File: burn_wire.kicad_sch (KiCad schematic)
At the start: 12 parts, among them Q4 Q_PI, Q5 TIP122, Q6 Q_NPN_BEC

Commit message: Edits to board post PDR.
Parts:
- added R21: 10 kohm, symbol Device:R_US
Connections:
- net GND: now also D7.1 (K)
- net at D5.2 (A2), Q5.2 (C), R8.1: now also R21.1
- net at D7.2 (A): now also R21.2
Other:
- note added: "LED on when Q5 is on (burn-wire active)."
- moved on the sheet: D7
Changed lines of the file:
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@@
+		)
+	)
+	(text "LED on when Q5 is on (burn-wire active)."
+		(exclude_from_sim no)
+		(at 153.162 83.312 0)
+		(effects
+			(font
+				(size 1.27 1.27)
+			)
 		)
 	)
@@
 		(color 0 0 0 0)
 	)
+	(junction
+		(at 116.84 78.74)
+		(diameter 0)
+		(color 0 0 0 0)
+	)
 	(wire
 		(pts
@@
 	(wire
 		(pts
+			(xy 116.84 78.74) (xy 116.84 87.63)
+		)
+		(stroke
+			(width 0)
+			(type default)
+		)
+	)
+	(wire
+		(pts
 			(xy 116.84 106.68) (xy 116.84 97.79)
 		)
@@
 	(wire
 		(pts
+			(xy 116.84 78.74) (xy 120.65 78.74)
+		)
+		(stroke
+			(width 0)
+			(type default)
+		)
+	)
+	(wire
+		(pts
 			(xy 54.61 74.93) (xy 54.61 95.25)
 		)
@@
 	(wire
 		(pts
+			(xy 128.27 78.74) (xy 133.35 78.74)
+		)
+		(stroke
+			(width 0)
+			(type default)
+		)
+	)
+	(wire
+		(pts
 			(xy 68.58 82.55) (xy 74.93 82.55)
 		)
@@
 	(wire
 		(pts
-			(xy 116.84 58.42) (xy 116.84 87.63)
+			(xy 140.97 78.74) (xy 148.59 78.74)
+		)
+		(stroke
+			(width 0)
+			(type default)
+		)
+	)
+	(wire
+		(pts
+			(xy 116.84 58.42) (xy 116.84 78.74)
 		)
 		(stroke
@@
 			(width 0)
 			(type default)
+		)
+	)
+	(global_label "GND"
+		(shape input)
+		(at 148.59 78.74 0)
+		(fields_autoplaced yes)
+		(effects
+			(font
+				(size 1.27 1.27)
+			)
+			(justify left)
+		)
+		(property "Intersheetrefs" "${INTERSHEET_REFS}"
+			(at 155.4457 78.74 0)
+			(effects
+				(font
+					(size 1.27 1.27)
+				)
+				(justify left)
+				(hide yes)
+			)
 		)
 	)
@@
 	)
 	(symbol
+		(lib_id "Device:R_US")
+		(at 124.46 78.74 90)
+		(unit 1)
+		(exclude_from_sim no)
+		(in_bom yes)
+		(on_board yes)
+		(dnp no)
+		(property "Reference" "R21"
+			(at 126.365 84.4551 90)
+			(effects
+				(font
+					(size 1.27 1.27)
+				)
+				(justify left)
+			)
+		)
+		(property "Value" "10 kohm"
+			(at 128.016 81.788 90)
+			(effects
+				(font
+					(size 1.27 1.27)
+				)
+				(justify left)
+			)
+		)
+		(property "Footprint" ""
+			(at 124.714 77.724 90)
+			(effects
+				(font
+					(size 1.27 1.27)
+				)
+				(hide yes)
+			)
+		)
+		(property "Datasheet" "~"
+			(at 124.46 78.74 0)
+			(effects
+				(font
+					(size 1.27 1.27)
+				)
+				(hide yes)
+			)
+		)
+		(property "Description" "Resistor, US symbol"
+			(at 124.46 78.74 0)
+			(effects
+				(font
+					(size 1.27 1.27)
+				)
+				(hide yes)
+			)
+		)
+		(pin "2"
+		)
+		(pin "1"
+		)
+		(instances
+			(project "deck_board"
+				(path "/0dd6c749-d328-44a2-b3d4-206fc5899db9/9a513996-12e6-4869-a836-62e374407735"
+					(reference "R21")
+					(unit 1)
+				)
+			)
+		)
+	)
+	(symbol
 		(lib_id "Transistor_BJT:Q_NPN_BEC")
 		(at 88.9 73.66 270)
@@
 	(symbol
 		(lib_id "Device:LED")
-		(at 127 50.8 0)
+		(at 137.16 78.74 180)
 		(unit 1)
 		(exclude_from_sim no)
@@
 		(fields_autoplaced yes)
 		(property "Reference" "D7"
-			(at 125.4125 44.45 0)
+			(at 138.7475 71.12 0)
 			(effects
 				(font
@@
 		)
 		(property "Value" "LED"
-			(at 125.4125 46.99 0)
+			(at 138.7475 73.66 0)
 			(effects
 				(font
@@
 		)
 		(property "Footprint" ""
-			(at 127 50.8 0)
+			(at 137.16 78.74 0)
 			(effects
 				(font
@@
 		)
 		(property "Datasheet" "~"
-			(at 127 50.8 0)
+			(at 137.16 78.74 0)
 			(effects
 				(font
@@
 		)
 		(property "Description" "Light emitting diode"
-			(at 127 50.8 0)
+			(at 137.16 78.74 0)
 			(effects
 				(font
@@
 		)
 		(property "Sim.Pins" "1=K 2=A"
-			(at 127 50.8 0)
-			(effects
-				(font
+			(at 137.16 78.74 0)
+			(effects
+				(font

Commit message: Updated files and include work done for PCB
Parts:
- D7: footprint (none) -> LED_SMD:LED_0603_1608Metric
- F3: footprint (none) -> Fuse:Fuse_1812_4532Metric
- Q4, Q6: footprint (none) -> Package_TO_SOT_SMD:SOT-23
- R10, R11, R12, R13, R14, R21, R8: footprint (none) -> Resistor_SMD:R_0201_0603Metric
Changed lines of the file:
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@@
 			)
 		)
-		(property "Footprint" ""
+		(property "Footprint" "Fuse:Fuse_1812_4532Metric"
 			(at 78.74 56.642 90)
 			(effects
@@
 			)
 		)
-		(property "Footprint" ""
+		(property "Footprint" "Resistor_SMD:R_0201_0603Metric"
 			(at 64.516 88.646 90)
 			(effects
@@
 			)
 		)
-		(property "Footprint" ""
+		(property "Footprint" "Resistor_SMD:R_0201_0603Metric"
 			(at 124.714 77.724 90)
 			(effects
@@
 			)
 		)
-		(property "Footprint" ""
+		(property "Footprint" "Package_TO_SOT_SMD:SOT-23"
 			(at 91.44 78.74 0)
 			(effects
@@
 			)
 		)
-		(property "Footprint" ""
+		(property "Footprint" "LED_SMD:LED_0603_1608Metric"
 			(at 137.16 78.74 0)
 			(effects
@@
 			)
 		)
-		(property "Footprint" ""
+		(property "Footprint" "Resistor_SMD:R_0201_0603Metric"
 			(at 64.516 83.566 90)
 			(effects
@@
 			)
 		)
-		(property "Footprint" ""
+		(property "Footprint" "Resistor_SMD:R_0201_0603Metric"
 			(at 96.266 59.436 90)
 			(effects
@@
 			)
 		)
-		(property "Footprint" ""
+		(property "Footprint" "Resistor_SMD:R_0201_0603Metric"
 			(at 77.216 93.726 90)
 			(effects
@@
 			)
 		)
-		(property "Footprint" ""
+		(property "Footprint" "Resistor_SMD:R_0201_0603Metric"
 			(at 96.774 98.806 90)
 			(effects
@@
 			)
 		)
-		(property "Footprint" ""
+		(property "Footprint" "Package_TO_SOT_SMD:SOT-23"
 			(at 77.47 72.39 0)
 			(effects
@@
 			)
 		)
-		(property "Footprint" ""
+		(property "Footprint" "Resistor_SMD:R_0201_0603Metric"
 			(at 55.626 99.314 90)
 			(effects

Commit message: PCB is mostly laid out, routing is WIP
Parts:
- removed D5: SMAJ33A, Diode_SMD:D_SMA, symbol Diode:SMAJ33A
- removed F3: Fuse, Fuse:Fuse_1812_4532Metric, symbol Device:Fuse
- removed Q4: Q_PI, Package_TO_SOT_SMD:SOT-23, symbol Transistor_BJT:Q_NPN_BEC
- removed Q5: TIP122, Package_TO_SOT_THT:TO-220-3_Vertical, symbol Transistor_BJT:TIP122
- removed Q6: Q_NPN_BEC, Package_TO_SOT_SMD:SOT-23, symbol Transistor_BJT:Q_NPN_BEC
- removed R12, R13, R14: R, Resistor_SMD:R_0201_0603Metric, symbol Device:R_US
- added C13: 0.1 µF, Capacitor_SMD:C_0603_1608Metric, symbol Device:C
- added F2: 1.0 A, Fuse:Fuse_1812_4532Metric, symbol Device:Fuse
- added Q5: NMOS, Package_TO_SOT_SMD:SOT-23, symbol Simulation_SPICE:NMOS
- added R24: 158Ω, Resistor_SMD:R_0201_0603Metric, symbol Device:R_US
- added R9: 100kΩ, Resistor_SMD:R_0201_0603Metric, symbol Device:R_US
- added U5: 74LVC1G08, Package_TO_SOT_SMD:SOT-23-5, symbol 74xGxx:74LVC1G08
- R10: value R -> 47Ω
- R11, R8: value R -> 100kΩ
- R21: value 10 kohm -> 10kΩ
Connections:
- net 3V_IN: now also U5.5 (VCC); no longer R10.2
- net CTRL_IN: now also R9.1, U5.1
- net ENABLE: now also R8.1, U5.2
- net GND: now also R8.2, C13.2, Q5.3 (S), R9.2; no longer D7.1 (K)
- net V_IN_28V: now also F2.2
- net at R21.1: now also R24.1; no longer R8.1
- net at R10.1, R11.2: now also Q5.2 (G)
- new net: D7.1 (K), Q5.1 (D)
- new net: C13.1, U5.3 (GND)
- new net: R10.2, U5.4
- new net: F2.1, R24.2
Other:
- note removed: "clamp transient voltage from burn element"
- note removed: "limit current"
- note removed: "low-side switch when base gets current, allows current to flow through R8"
- note removed: "pull-up"
- note removed: "when pi outputs high, conducts"
- note removed: "when signal from inhibit is high, conducts"

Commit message: Finished PCB, ready to print
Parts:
- added J2, J3: Conn_01x01_Pin, Connector_Wire:SolderWire-0.75sqmm_1x01_D1.25mm_OD2.3mm, symbol Connector:Conn_01x01_Pin
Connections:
- net at R21.1, R24.1: now also J3.1 (Pin_1)
- net at F2.1, R24.2: now also J2.1 (Pin_1)
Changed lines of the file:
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@@
+	)
+	(junction
+		(at 90.17 52.07)
+		(diameter 0)
+		(color 0 0 0 0)
 	)
 	(junction
@@
 	)
 	(junction
+		(at 110.49 52.07)
+		(diameter 0)
+		(color 0 0 0 0)
+	)
+	(junction
 		(at 119.38 95.25)
 		(diameter 0)
@@
 	(wire
 		(pts
+			(xy 90.17 52.07) (xy 97.79 52.07)
+		)
+		(stroke
+			(width 0)
+			(type default)
+		)
+	)
+	(wire
+		(pts
 			(xy 119.38 88.9) (xy 119.38 95.25)
 		)
@@
 	(wire
 		(pts
-			(xy 60.96 52.07) (xy 97.79 52.07)
+			(xy 60.96 52.07) (xy 90.17 52.07)
 		)
 		(stroke
@@
 	(wire
 		(pts
+			(xy 110.49 50.8) (xy 110.49 52.07)
+		)
+		(stroke
+			(width 0)
+			(type default)
+		)
+	)
+	(wire
+		(pts
 			(xy 101.6 74.93) (xy 105.41 74.93)
 		)
@@
 	(wire
 		(pts
+			(xy 110.49 52.07) (xy 105.41 52.07)
+		)
+		(stroke
+			(width 0)
+			(type default)
+		)
+	)
+	(wire
+		(pts
 			(xy 133.35 60.96) (xy 133.35 59.69)
 		)
@@
 	(wire
 		(pts
+			(xy 90.17 50.8) (xy 90.17 52.07)
+		)
+		(stroke
+			(width 0)
+			(type default)
+		)
+	)
+	(wire
+		(pts
 			(xy 69.85 87.63) (xy 69.85 95.25)
 		)
@@
 	(wire
 		(pts
-			(xy 133.35 52.07) (xy 105.41 52.07)
+			(xy 133.35 52.07) (xy 110.49 52.07)
 		)
 		(stroke
@@
 			)
 			(justify right)
+		)
+	)
+	(symbol
+		(lib_id "Connector:Conn_01x01_Pin")
+		(at 110.49 45.72 270)
+		(unit 1)
+		(exclude_from_sim no)
+		(in_bom yes)
+		(on_board yes)
+		(dnp no)
+		(fields_autoplaced yes)
+		(property "Reference" "J3"
+			(at 111.76 45.0849 90)
+			(effects
+				(font
+					(size 1.27 1.27)
+				)
+				(justify left)
+			)
+		)
+		(property "Value" "Conn_01x01_Pin"
+			(at 111.76 47.6249 90)
+			(effects
+				(font
+					(size 1.27 1.27)
+				)
+				(justify left)
+			)
+		)
+		(property "Footprint" "Connector_Wire:SolderWire-0.75sqmm_1x01_D1.25mm_OD2.3mm"
+			(at 110.49 45.72 0)
+			(effects
+				(font
+					(size 1.27 1.27)
+				)
+				(hide yes)
+			)
+		)
+		(property "Datasheet" "~"
+			(at 110.49 45.72 0)
+			(effects
+				(font
+					(size 1.27 1.27)
+				)
+				(hide yes)
+			)
+		)
+		(property "Description" "Generic connector, single row, 01x01, script generated"
+			(at 110.49 45.72 0)
+			(effects
+				(font
+					(size 1.27 1.27)
+				)
+				(hide yes)
+			)
+		)
+		(pin "1"
+		)
+		(instances
+			(project "deck_boardv1.2"
+				(path "/0dd6c749-d328-44a2-b3d4-206fc5899db9/9a513996-12e6-4869-a836-62e374407735"
+					(reference "J3")
+					(unit 1)
+				)
+			)
 		)
 	)
@@
 					(unit 1)
 				)
+			)
+		)
+	)
+	(symbol
+		(lib_id "Connector:Conn_01x01_Pin")
+		(at 90.17 45.72 270)
+		(unit 1)
+		(exclude_from_sim no)
+		(in_bom yes)
+		(on_board yes)
+		(dnp no)
+		(fields_autoplaced yes)
+		(property "Reference" "J2"
+			(at 91.44 45.0849 90)
+			(effects
+				(font
+					(size 1.27 1.27)
+				)
+				(justify left)
+			)
+		)
+		(property "Value" "Conn_01x01_Pin"
+			(at 91.44 47.6249 90)
+			(effects
+				(font
+					(size 1.27 1.27)
+				)
+				(justify left)
+			)
+		)
+		(property "Footprint" "Connector_Wire:SolderWire-0.75sqmm_1x01_D1.25mm_OD2.3mm"
+			(at 90.17 45.72 0)
+			(effects
+				(font
+					(size 1.27 1.27)
+				)
+				(hide yes)
+			)
+		)
+		(property "Datasheet" "~"
+			(at 90.17 45.72 0)
+			(effects
+				(font
+					(size 1.27 1.27)
+				)
+				(hide yes)
+			)
+		)
+		(property "Description" "Generic connector, single row, 01x01, script generated"
+			(at 90.17 45.72 0)
+			(effects
+				(font
+					(size 1.27 1.27)
+				)
+				(hide yes)
+			)
+		)
+		(pin "1"
+		)
+		(instances
+			(project ""
+				(path "/0dd6c749-d328-44a2-b3d4-206fc5899db9/9a513996-12e6-4869-a836-62e374407735"
+					(reference "J2")
+					(unit 1)
+				)

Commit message: Made changes to schematic
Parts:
- removed C13: 0.1 µF, Capacitor_SMD:C_0603_1608Metric, symbol Device:C
- removed F2: 1.0 A, Fuse:Fuse_1812_4532Metric, symbol Device:Fuse
- removed R10: 47Ω, Resistor_SMD:R_0201_0603Metric, symbol Device:R_US
- removed R11, R8, R9: 100kΩ, Resistor_SMD:R_0201_0603Metric, symbol Device:R_US
- removed U5: 74LVC1G08, Package_TO_SOT_SMD:SOT-23-5, symbol 74xGxx:74LVC1G08
- added R2: 100kΩ, Resistor_SMD:R_0201_0603Metric, symbol Device:R_US
- R21: value 10kΩ -> 1.8kΩ
- R24: value 158Ω -> 56Ω
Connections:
- net ENABLE: now also J2.1 (Pin_1), Q5.2 (G), R21.1, R24.2, R2.2
- net GND: now also D7.1 (K), R2.1
- net at J3.1 (Pin_1), R24.1: now also Q5.1 (D); no longer R21.1
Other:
- moved on the sheet: D7, J2, J3, Q5, R21, R24

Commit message: adjustments have been made, PCB is also done
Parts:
- renumbered D7 to D6, Q5 to Q3, R21 to R14, R24 to R15, R2 to R16
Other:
- note added: "LED on when Q3 is on (burn-wire active)."
- note removed: "LED on when Q5 is on (burn-wire active)."
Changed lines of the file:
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@@
 	(generator_version "9.0")
 	(paper "A4")
-	(text "LED on when Q5 is on (burn-wire active)."
+	(text "LED on when Q3 is on (burn-wire active)."
 		(exclude_from_sim no)
 		(at 109.728 39.37 0)
@@
 		)
 	)
+	(hierarchical_label "GND"
+		(shape input)
+		(at 54.61 90.17 180)
+		(effects
+			(font
+				(size 1.27 1.27)
+			)
+			(justify right)
+		)
+	)
 	(symbol
 		(lib_id "Connector:Conn_01x01_Pin")
@@
 		(dnp no)
 		(fields_autoplaced yes)
-		(property "Reference" "Q5"
+		(property "Reference" "Q3"
 			(at 85.09 88.8999 0)
 			(effects
@@
 			(project "deck_boardv1.1"
 				(path "/0dd6c749-d328-44a2-b3d4-206fc5899db9/9a513996-12e6-4869-a836-62e374407735"
-					(reference "Q5")
+					(reference "Q3")
 					(unit 1)
 				)
@@
 		(on_board yes)
 		(dnp no)
-		(property "Reference" "R2"
+		(property "Reference" "R16"
 			(at 62.23 96.52 90)
 			(effects
@@
 			(project "deck_boardv1.3"
 				(path "/0dd6c749-d328-44a2-b3d4-206fc5899db9/9a513996-12e6-4869-a836-62e374407735"
-					(reference "R2")
+					(reference "R16")
 					(unit 1)
 				)
@@
 		(on_board yes)
 		(dnp no)
-		(property "Reference" "D7"
+		(property "Reference" "D6"
 			(at 108.585 42.8624 0)
 			(effects
@@
 			(project "deck_boardv1.1"
 				(path "/0dd6c749-d328-44a2-b3d4-206fc5899db9/9a513996-12e6-4869-a836-62e374407735"
-					(reference "D7")
+					(reference "D6")
 					(unit 1)
 				)
@@
 		(on_board yes)
 		(dnp no)
-		(property "Reference" "R21"
+		(property "Reference" "R14"
 			(at 102.489 45.847 90)
 			(effects
@@
 			(project "deck_boardv1.1"
 				(path "/0dd6c749-d328-44a2-b3d4-206fc5899db9/9a513996-12e6-4869-a836-62e374407735"
-					(reference "R21")
-					(unit 1)
-				)
-			)
-		)
-	)
-	(symbol
-		(lib_id "power:GND")
-		(at 54.61 90.17 270)
-		(unit 1)
-		(exclude_from_sim no)
-		(in_bom yes)
-		(on_board yes)
-		(dnp no)
-		(property "Reference" "#PWR034"
-			(at 48.26 90.17 0)
-			(effects
-				(font
-					(size 1.27 1.27)
-				)
-				(hide yes)
-			)
-		)
-		(property "Value" "GND"
-			(at 50.546 90.17 0)
-			(effects
-				(font
-					(size 1.27 1.27)
-				)
-			)
-		)
-		(property "Footprint" ""
-			(at 54.61 90.17 0)
-			(effects
-				(font
-					(size 1.27 1.27)
-				)
-				(hide yes)
-			)
-		)
-		(property "Datasheet" ""
-			(at 54.61 90.17 0)
-			(effects
-				(font
-					(size 1.27 1.27)
-				)
-				(hide yes)
-			)
-		)
-		(property "Description" "Power symbol creates a global label with name \"GND\" , ground"
-			(at 54.61 90.17 0)
-			(effects
-				(font
-					(size 1.27 1.27)
-				)
-				(hide yes)
-			)
-		)
-		(pin "1"
-		)
-		(instances
-			(project "deck_boardv1.3"
-				(path "/0dd6c749-d328-44a2-b3d4-206fc5899db9/9a513996-12e6-4869-a836-62e374407735"
-					(reference "#PWR034")
+					(reference "R14")
 					(unit 1)
 				)
@@
 		(on_board yes)
 		(dnp no)
-		(property "Reference" "R24"
+		(property "Reference" "R15"
 			(at 86.36 66.04 0)
 			(effects
@@
 			(project "deck_boardv1.1"
 				(path "/0dd6c749-d328-44a2-b3d4-206fc5899db9/9a513996-12e6-4869-a836-62e374407735"
-					(reference "R24")
+					(reference "R15")
 					(unit 1)
 				)

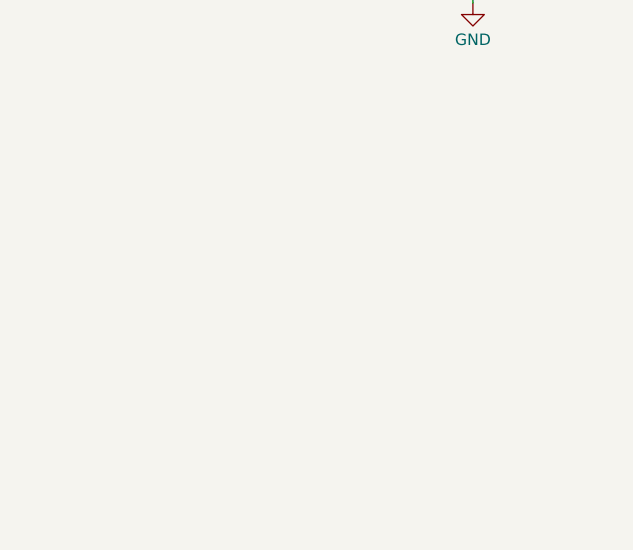
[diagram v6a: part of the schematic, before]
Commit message: Resolved errors and warnings.
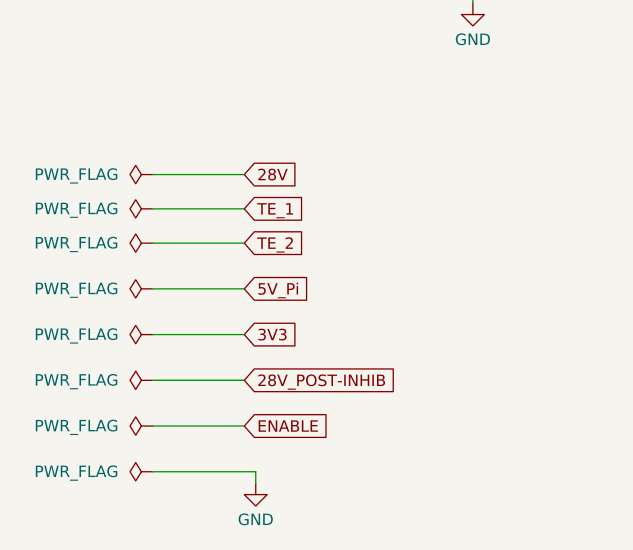
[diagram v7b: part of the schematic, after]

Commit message: Made board smaller.
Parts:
- R14, R15, R16: footprint Resistor_SMD:R_0201_0603Metric -> Resistor_SMD:R_0603_1608Metric
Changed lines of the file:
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@@
 			)
 		)
-		(property "Footprint" "Resistor_SMD:R_0201_0603Metric"
+		(property "Footprint" "Resistor_SMD:R_0603_1608Metric"
 			(at 62.484 89.154 90)
 			(effects
@@
 			)
 		)
-		(property "Footprint" "Resistor_SMD:R_0201_0603Metric"
+		(property "Footprint" "Resistor_SMD:R_0603_1608Metric"
 			(at 100.584 48.514 90)
 			(effects
@@
 			)
 		)
-		(property "Footprint" "Resistor_SMD:R_0201_0603Metric"
+		(property "Footprint" "Resistor_SMD:R_0603_1608Metric"
 			(at 80.264 67.056 90)
 			(effects
